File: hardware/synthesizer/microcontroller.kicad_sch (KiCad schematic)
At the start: 3 parts, among them J9 Conn_ARM_JTAG_SWD_10, U4 STM32H723VGTx

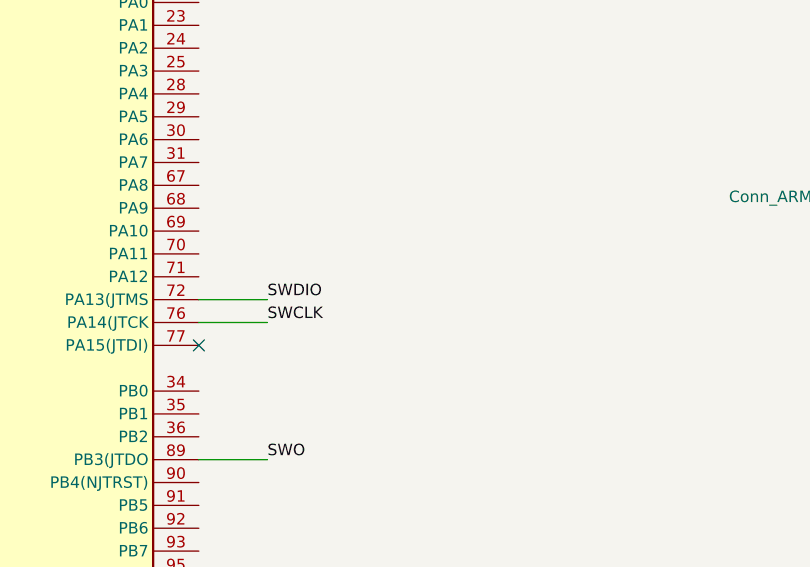
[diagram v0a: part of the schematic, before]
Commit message: start connecting sheets
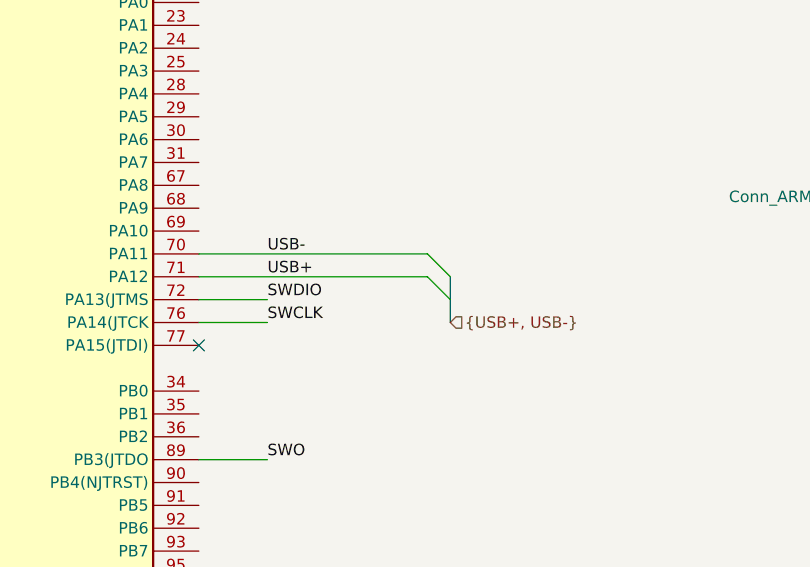
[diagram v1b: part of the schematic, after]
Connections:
- net USB-: now reaches U4.70 (PA11)
- net USB+: now reaches U4.71 (PA12)

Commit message: work on hardware
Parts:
- added C1, C2, C3, C8: 100n/50V, symbol Device:C
- added C7: 1u/16V, symbol Device:C
- added C9, C?: 10p/50V, symbol Device:C
- added C?: 10u/10V, symbol Device:C
- added D1: Yellow, symbol Device:LED
- added D3: Green, symbol Device:LED
- added D?: Red, symbol Device:LED
- added J10: RJ45_Abracon_ARJP11A-MASA-B-A-EMU2, Connector_RJ:RJ45_Abracon_ARJP11A-MA_Horizontal, symbol Connector:RJ45_Abracon_ARJP11A-MASA-B-A-EMU2
- added R1, R2, R?: 1k, symbol Device:R
- added R?: 10k, symbol Device:R
- added TP?: VREF, symbol Connector:TestPoint
- added Y?: 16MHz/8pF, symbol Device:Crystal_GND24
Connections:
- net +3.3V: now also U4.100 (VDD), U4.11 (VDD), U4.21 (VDDA), U4.27 (VDD), U4.50 (VDD), U4.6 (VBAT), U4.75 (VDD), C1.1, C2.1, C3.1, C?.1, J10.9 (V+), R?.1
- net GND: now also U4.94 (BOOT0), C1.2, C2.2, C3.2, C7.2, C8.2, C9.2, C?.2, C?.2, D1.1 (K), D3.1 (K), D?.1 (K), J10.10 (V-), Y?.2, Y?.4
- net OSC_IN: now reaches U4.12 (PH0)
- net OSC_IN: now also C9.1, Y?.1
- net OSC_OUT: now reaches U4.13 (PH1)
- net OSC_OUT: now also C?.1, Y?.3
- net at U4.14 (NRST): now also R?.2
- net at U4.20 (VREF+): now also C7.1, C8.1, TP?.1
- net LED1: now reaches U4.34 (PB0)
- net LED1: now also R?.1
- net LED2: now reaches U4.35 (PB1)
- net LED2: now also R1.1
- net LED3: now reaches U4.36 (PB2)
- net LED3: now also R2.1
- new net: D3.2 (A), R?.2
- new net: D1.2 (A), R1.2
- new net: D?.2 (A), R2.2
- no-connect marks 2 -> 3
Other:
- moved on the sheet: U4

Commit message: update synthesizer
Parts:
- added C10: 1uF/10V, symbol Device:C
- added C11: 470pF/10V, symbol Device:C
- added R10, R11, R?: 10k, symbol Device:R
- added R12: 5.6k, symbol Device:R
- added R7, R8, R9, R?: 49.9k, symbol Device:R
- added R?: 100k, symbol Device:R
- added U?: LAN8742A, Package_DFN_QFN:VQFN-24-1EP_4x4mm_P0.5mm_EP2.5x2.5mm_ThermalVias, symbol Interface_Ethernet:LAN8742A
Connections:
- net +3.3V: now also R10.1, R7.1, R8.1, R9.1, R?.1, R?.1, U?.1 (VDD2A), U?.19 (VDD1A), U?.9 (VDDIO); no longer J10.9 (V+)
- net GND: now also C10.2, C11.2, R11.2, R12.2, R?.2, U?.25 (VSS); no longer J10.10 (V-)
- new net: R?.1, U?.10 (RXER/PHYAD0)
- new net: R11.1, U?.2 (LED2/~{INTSEL})
- new net: R12.1, U?.24 (RBIAS)
- new net: R10.2, U?.3 (LED1/REGOFF)
- new net +1.2V: C10.1, C11.1, U?.6 (VDDCR)
- new net 25MHz: U?.5 (XTAL1/CLKIN)
- new net ET_MDC: U?.13 (MDC)
- new net ET_MDIO: U?.12 (MDIO)
- new net ET_RCLK: U?.14 (~{INT}/REFCLKO)
- new net ET_RX0: U?.8 (RXD0/MODE0)
- new net ET_RX1: U?.7 (RXD1/MODE1)
- new net ET_TX0: U?.17 (TXD0)
- new net ET_TX1: U?.18 (TXD1)
- new net ET_TXEN: U?.16 (TXEN)
- new net RST_ETH: R?.2, U?.15 (~{RST})
- new net RX_N: R?.2, U?.22 (RXN)
- new net RX_P: R7.2, U?.23 (RXP)
- new net TX_N: R8.2, U?.20 (TXN)
- new net TX_P: R9.2, U?.21 (TXP)
- no-connect marks 3 -> 4
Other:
- moved on the sheet: C1, C2, C3, C7, C8, C9, C?, D1, D3, D7, D?, J9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

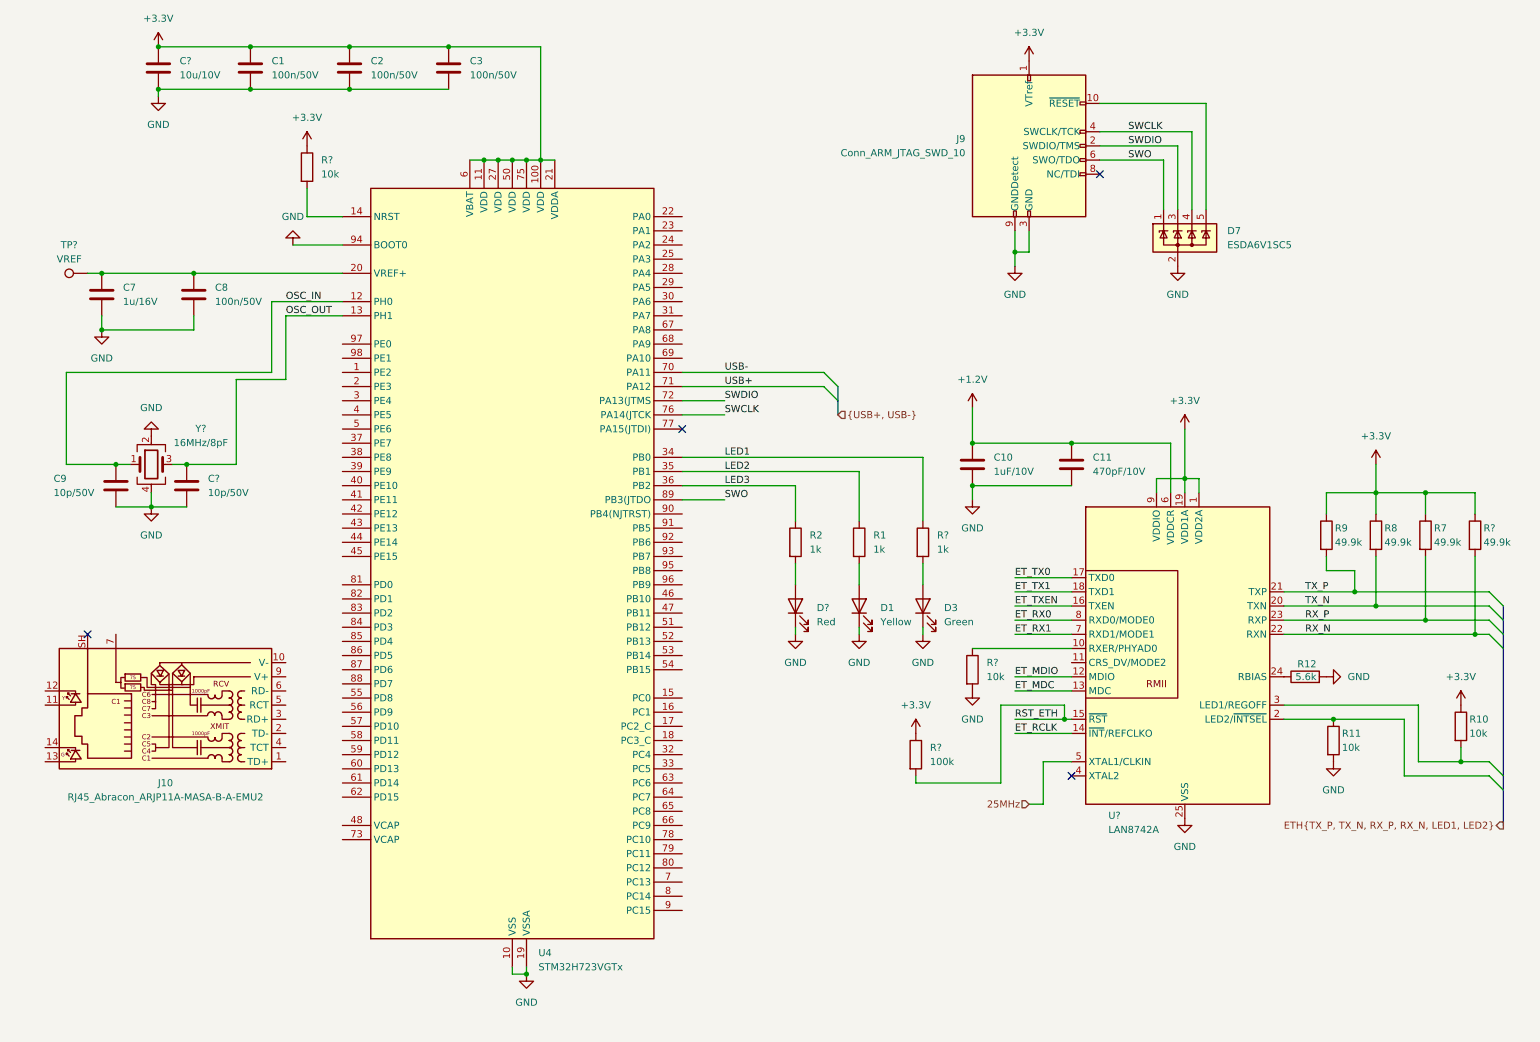
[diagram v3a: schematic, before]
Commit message: finish ethernet jack
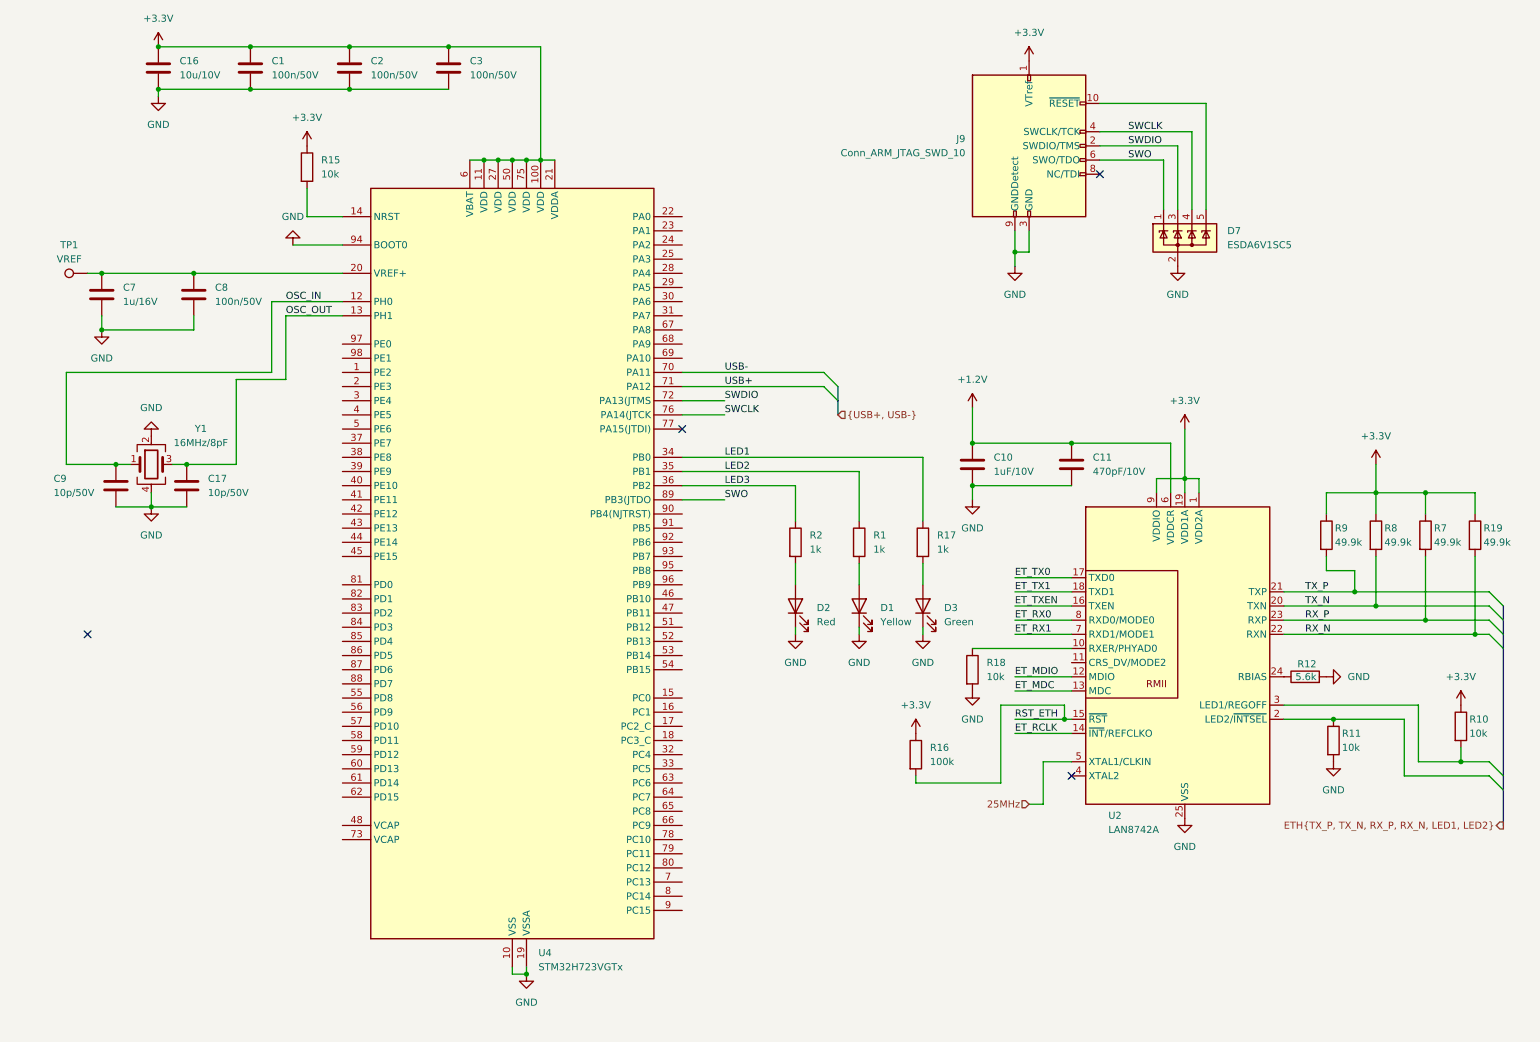
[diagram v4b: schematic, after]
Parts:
- removed J10: RJ45_Abracon_ARJP11A-MASA-B-A-EMU2, Connector_RJ:RJ45_Abracon_ARJP11A-MA_Horizontal, symbol Connector:RJ45_Abracon_ARJP11A-MASA-B-A-EMU2
- gave numbers to parts that had none: 11

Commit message: clean up synthesizer schematics
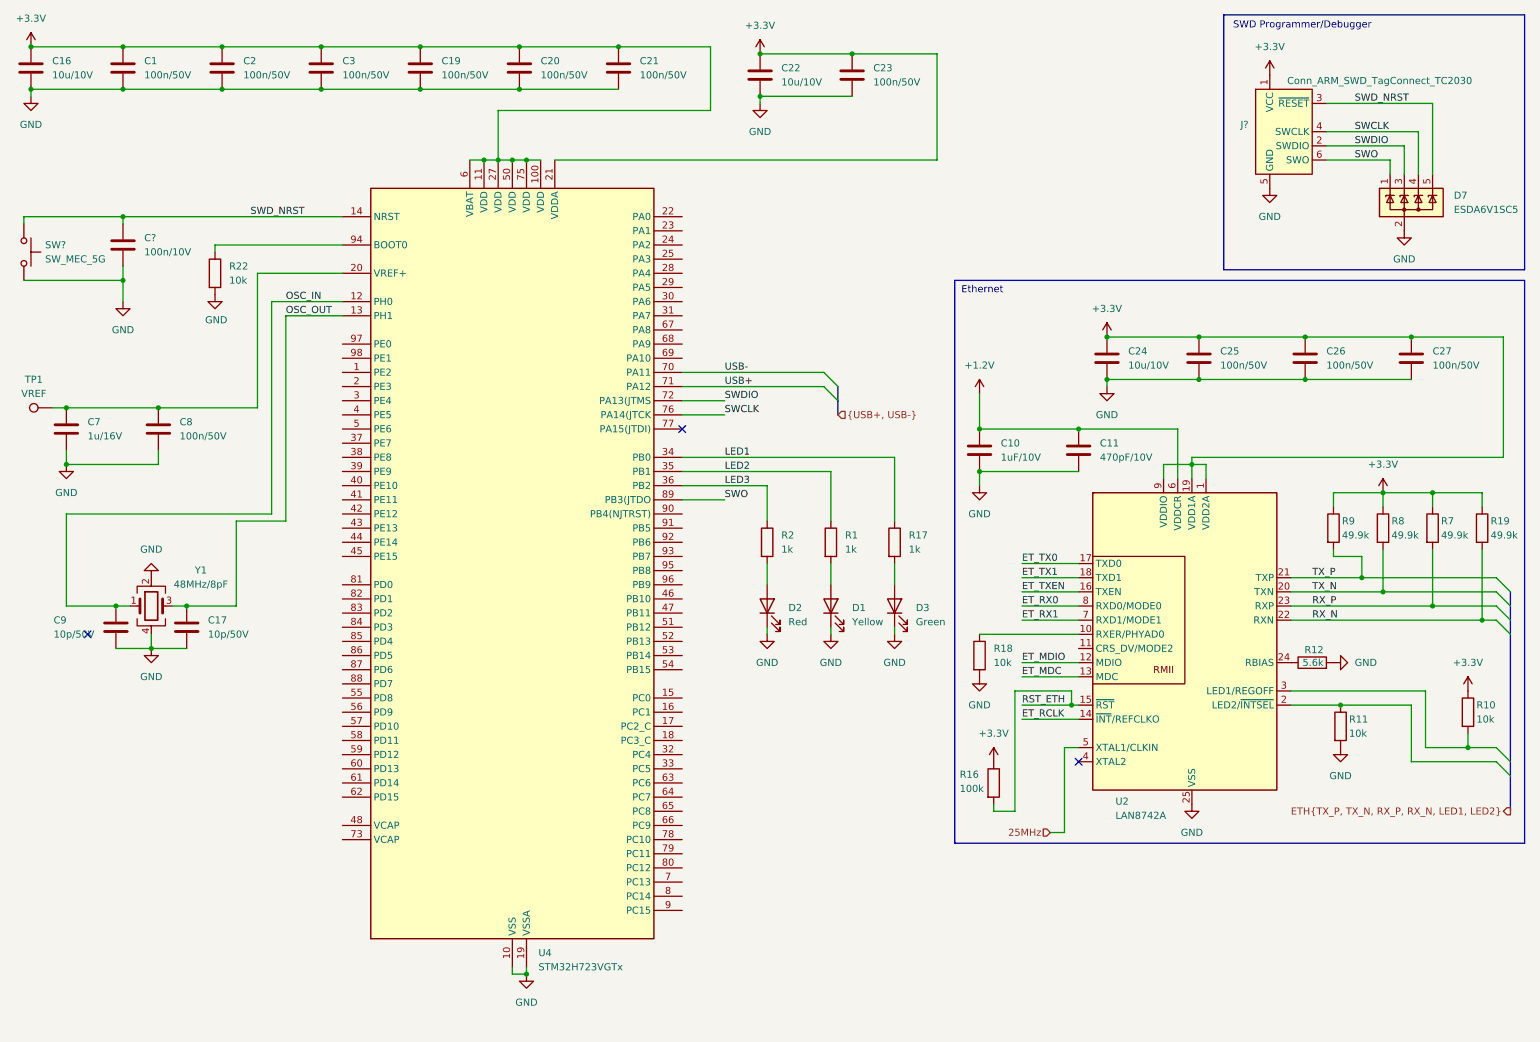
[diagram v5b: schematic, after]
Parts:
- removed J9: Conn_ARM_JTAG_SWD_10, Connector_PinHeader_1.27mm:PinHeader_2x05_P1.27mm_Vertical, symbol Connector:Conn_ARM_JTAG_SWD_10
- removed R15: 10k, symbol Device:R
- added C19, C20, C21, C23, C25, C26, C27: 100n/50V, symbol Device:C
- added C22, C24: 10u/10V, symbol Device:C
- added C?: 100n/10V, symbol Device:C
- added J?: Conn_ARM_SWD_TagConnect_TC2030, Connector:Tag-Connect_TC2030-IDC-FP_2x03_P1.27mm_Vertical, symbol Connector:Conn_ARM_SWD_TagConnect_TC2030
- added R22: 10k, symbol Device:R
- added SW?: SW_MEC_5G, symbol Switch:SW_MEC_5G
- Y1: value 16MHz/8pF -> 48MHz/8pF
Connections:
- net +3.3V: now also C19.1, C20.1, C21.1, C22.1, C23.1, C24.1, C25.1, C26.1, C27.1, J?.1 (VCC)
- net GND: now also C19.2, C20.2, C21.2, C22.2, C23.2, C24.2, C25.2, C26.2, C27.2, C?.2, J?.5 (GND), R22.2, SW?.3 (B), SW?.4 (B); no longer U4.94 (BOOT0)
- net SWCLK: now also J?.4 (SWCLK)
- net SWDIO: now also J?.2 (SWDIO)
- net SWO: now also J?.6 (SWO)
- net SWD_NRST: now reaches D7.5 (K)
- net SWD_NRST: now also U4.14 (NRST), C?.1, J?.3 (~{RESET}), SW?.1 (A), SW?.2 (A)
- new net: R22.1, U4.94 (BOOT0)
- no-connect marks 4 -> 3
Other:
- note added: "Ethernet"
- note added: "SWD Programmer/Debugger"
- moved on the sheet: C1, C10, C11, C16, C17, C2, C3, C7, C8, C9, D1, D2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

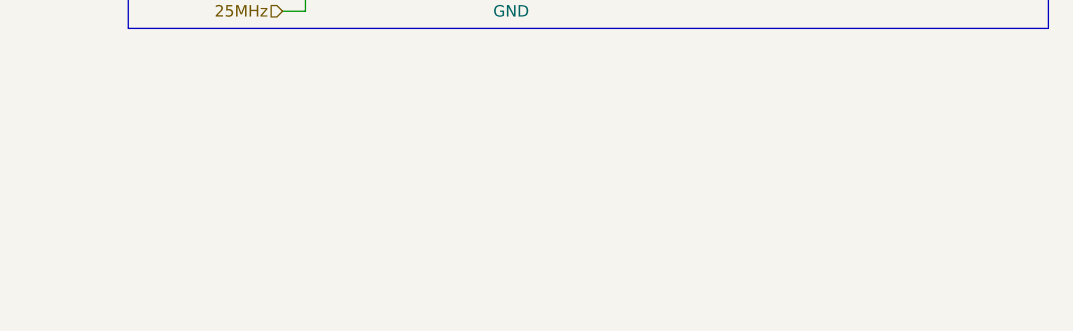
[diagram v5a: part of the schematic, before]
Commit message: add logo to every sheet
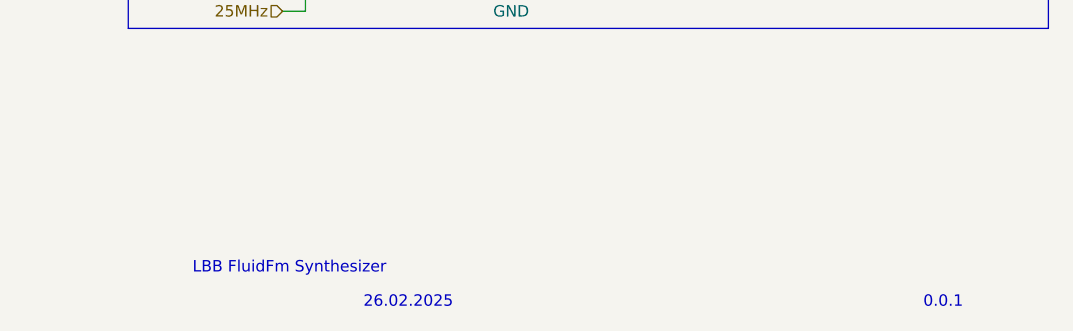
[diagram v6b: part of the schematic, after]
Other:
- note added: "0.0.1"
- note added: "26.02.2025"
- note added: "LBB FluidFm Synthesizer"
